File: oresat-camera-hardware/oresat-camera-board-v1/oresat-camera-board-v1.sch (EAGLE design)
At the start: 41 parts, among them J1 4-1734742-0, U1 AR0134CSSM00SPCA0, U2 TPS70618DRVR, U3 TPS71928-28DRVT, U4 TPS71928-28DRVT, X1 KC2520B27.0000C10E00

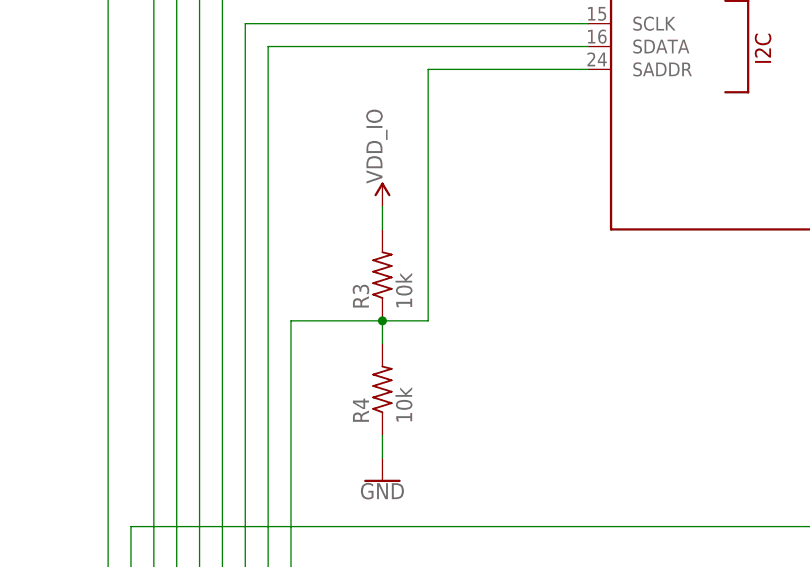
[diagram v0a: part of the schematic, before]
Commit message: small aesthetic changes
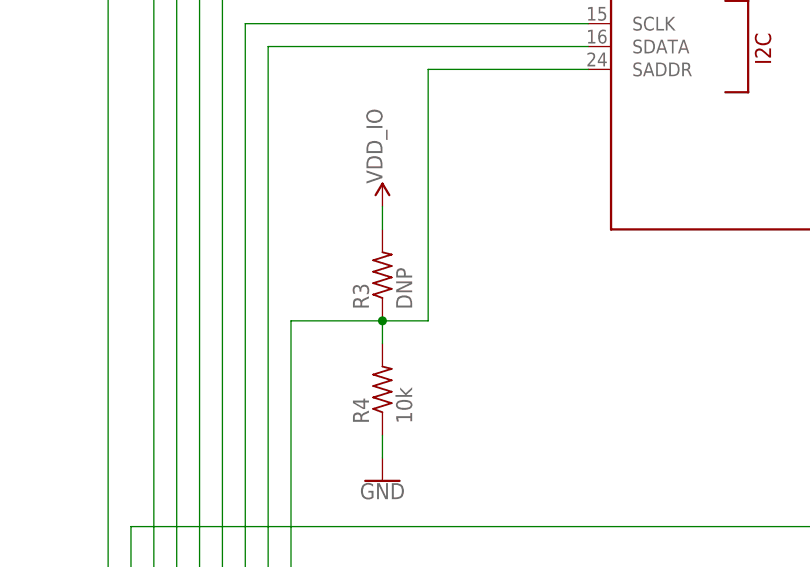
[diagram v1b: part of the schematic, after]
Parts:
- R3: value 10k -> DNP
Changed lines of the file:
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@@
 <part name="U1" library="U-ONSemi-AR0134" deviceset="AR0134CSSM00SPCA0" device=""/>
 <part name="GND6" library="SparkFun-PowerSymbols" deviceset="GND" device=""/>
-<part name="R3" library="oresat-rcl" deviceset="R-US_" device="0402-B" value="10k"/>
+<part name="R3" library="oresat-rcl" deviceset="R-US_" device="0402-B" value="DNP"/>
 <part name="SUPPLY3" library="SparkFun-PowerSymbols" deviceset="2.8V" device="" value="2.8V_1"/>
 <part name="R4" library="oresat-rcl" deviceset="R-US_" device="0402-B" value="10k"/>

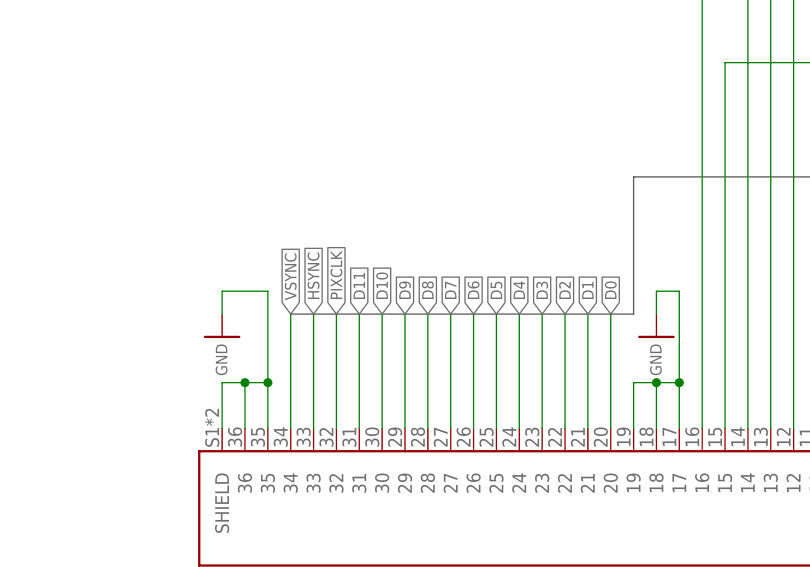
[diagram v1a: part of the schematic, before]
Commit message: rerouted camera bus
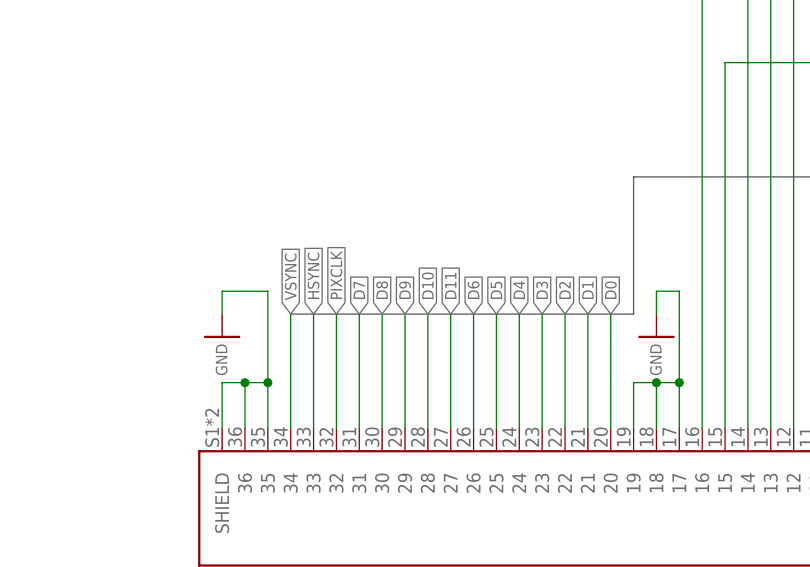
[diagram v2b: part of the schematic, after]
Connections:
- net D10: now also J1.28; no longer J1.30
- net D11: now also J1.27; no longer J1.31
- net D7: now also J1.31; no longer J1.27
- net D8: now also J1.30; no longer J1.28
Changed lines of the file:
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@@
 </segment>
 <segment>
-<pinref part="J1" gate="G$1" pin="27"/>
-<wire x1="109.22" y1="111.76" x2="109.22" y2="99.06" width="0.1524" layer="91"/>
-<label x="109.22" y="111.76" size="1.27" layer="95" rot="R90" xref="yes"/>
+<pinref part="J1" gate="G$1" pin="31"/>
+<wire x1="99.06" y1="111.76" x2="99.06" y2="99.06" width="0.1524" layer="91"/>
+<label x="99.06" y="111.76" size="1.27" layer="95" rot="R90" xref="yes"/>
 </segment>
 </net>
@@
 </segment>
 <segment>
-<pinref part="J1" gate="G$1" pin="28"/>
-<wire x1="106.68" y1="111.76" x2="106.68" y2="99.06" width="0.1524" layer="91"/>
-<label x="106.68" y="111.76" size="1.27" layer="95" rot="R90" xref="yes"/>
+<pinref part="J1" gate="G$1" pin="30"/>
+<wire x1="101.6" y1="111.76" x2="101.6" y2="99.06" width="0.1524" layer="91"/>
+<label x="101.6" y="111.76" size="1.27" layer="95" rot="R90" xref="yes"/>
 </segment>
 </net>
@@
 </segment>
 <segment>
-<pinref part="J1" gate="G$1" pin="30"/>
-<wire x1="101.6" y1="111.76" x2="101.6" y2="99.06" width="0.1524" layer="91"/>
-<label x="101.6" y="111.76" size="1.27" layer="95" rot="R90" xref="yes"/>
+<pinref part="J1" gate="G$1" pin="28"/>
+<wire x1="106.68" y1="111.76" x2="106.68" y2="99.06" width="0.1524" layer="91"/>
+<label x="106.68" y="111.76" size="1.27" layer="95" rot="R90" xref="yes"/>
 </segment>
 </net>
@@
 </segment>
 <segment>
-<pinref part="J1" gate="G$1" pin="31"/>
-<wire x1="99.06" y1="111.76" x2="99.06" y2="99.06" width="0.1524" layer="91"/>
-<label x="99.06" y="111.76" size="1.27" layer="95" rot="R90" xref="yes"/>
+<pinref part="J1" gate="G$1" pin="27"/>
+<wire x1="109.22" y1="111.76" x2="109.22" y2="99.06" width="0.1524" layer="91"/>
+<label x="109.22" y="111.76" size="1.27" layer="95" rot="R90" xref="yes"/>
 </segment>
 </net>

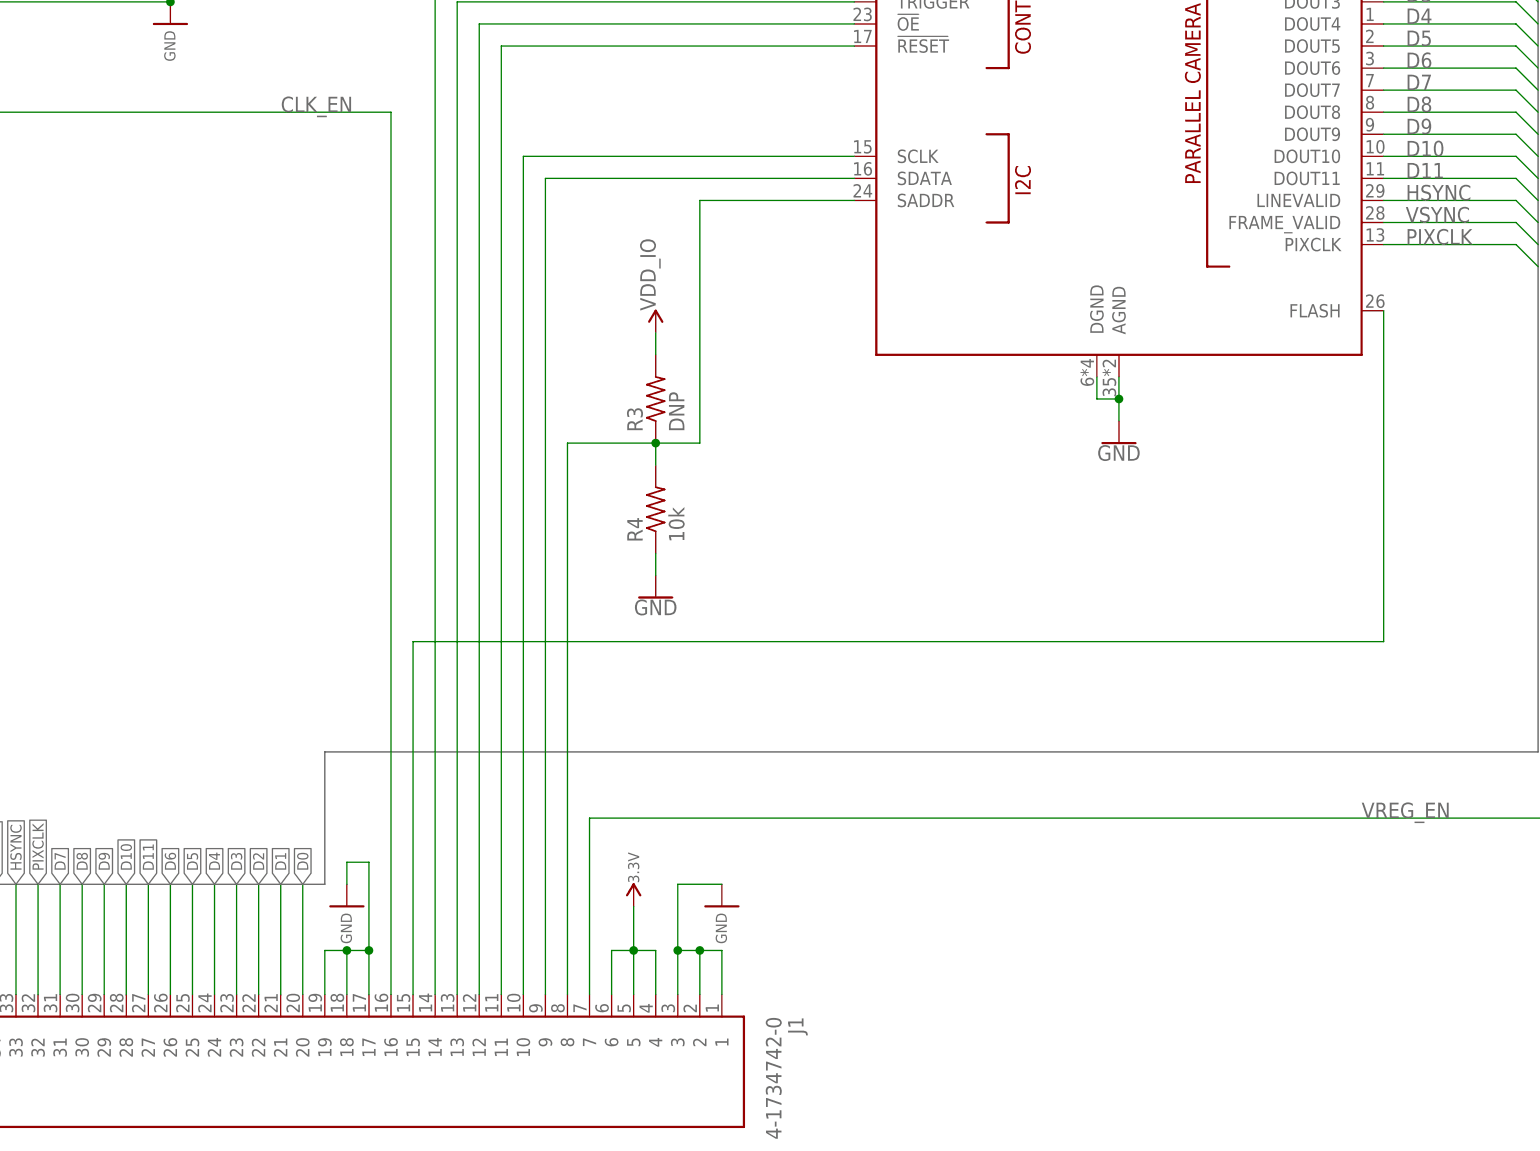
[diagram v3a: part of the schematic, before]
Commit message: added i2c pullups
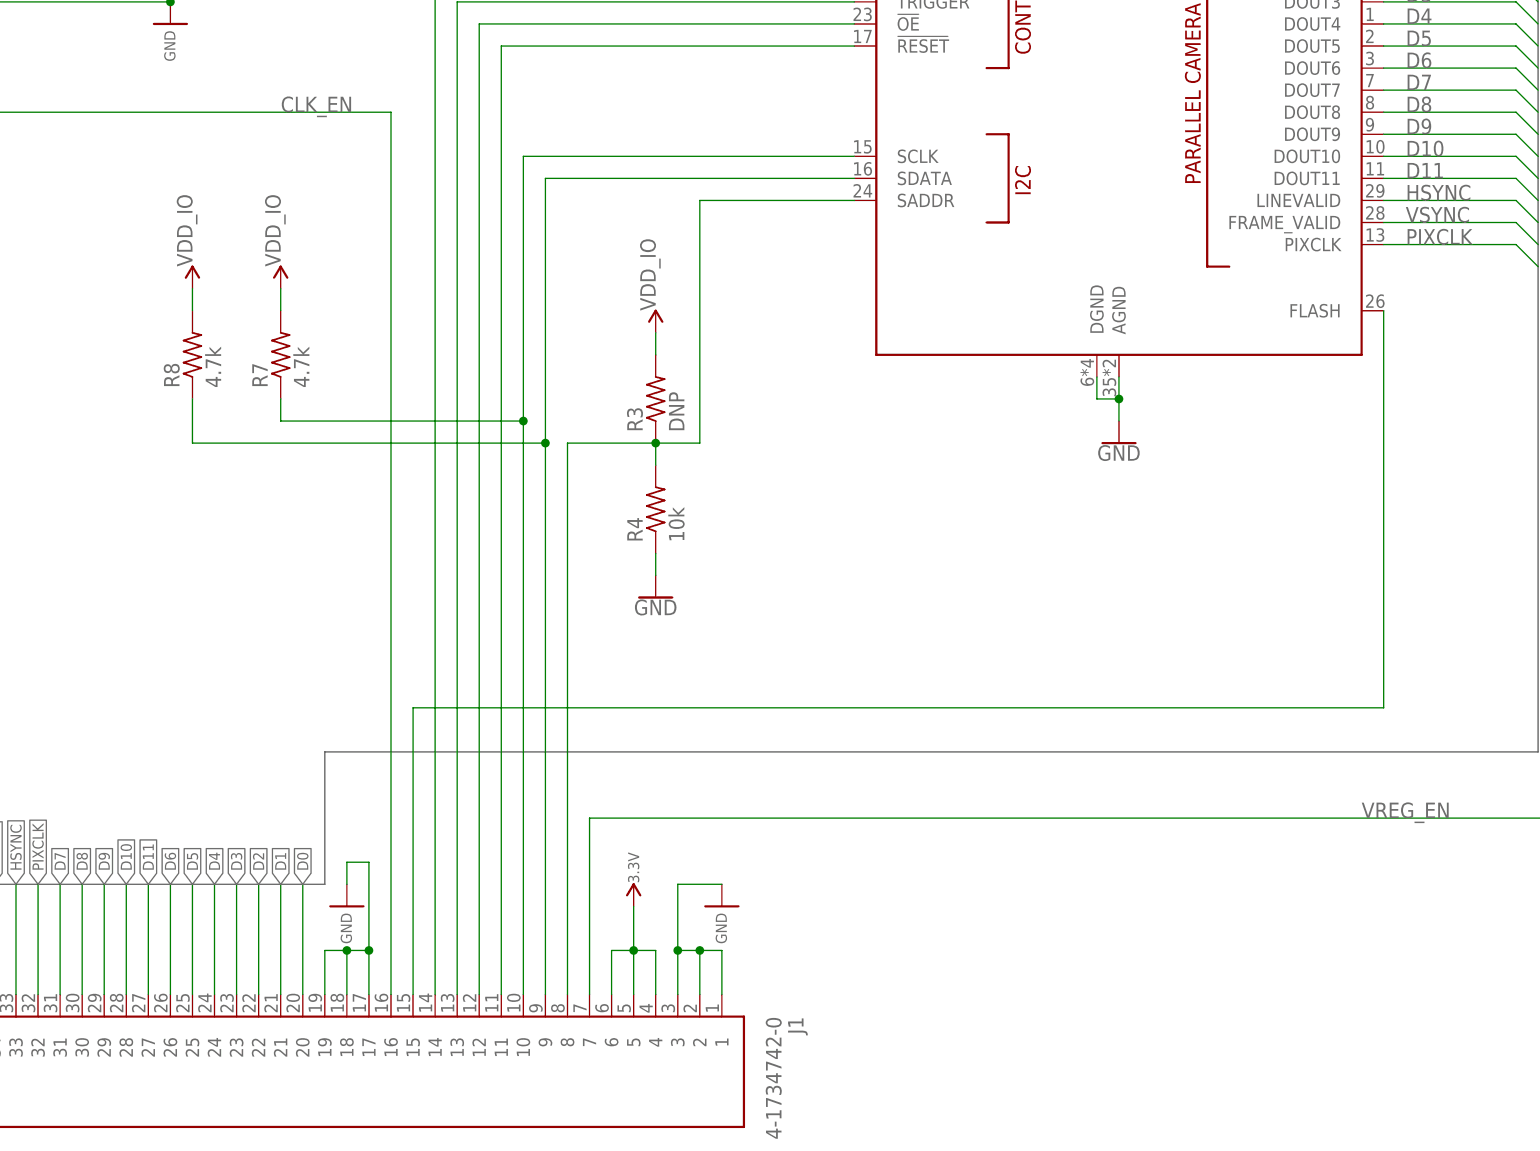
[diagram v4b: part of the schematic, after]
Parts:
- added R7, R8: 4.7k, oresat-rcl:R-US_0402-B
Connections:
- net N$3: now also R8.1
- net N$4: now also R7.1
- net VDD_IO: now also R7.2, R8.2
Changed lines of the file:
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@@
 <part name="SUPPLY27" library="SparkFun-PowerSymbols" deviceset="VCC_1" device="" value="2.8V_3"/>
 <part name="SUPPLY30" library="SparkFun-PowerSymbols" deviceset="VCC_2" device="" value="2.8V_4"/>
+<part name="R7" library="oresat-rcl" deviceset="R-US_" device="0402-B" value="4.7k"/>
+<part name="SUPPLY34" library="SparkFun-PowerSymbols" deviceset="2.8V" device="" value="2.8V_1"/>
+<part name="R8" library="oresat-rcl" deviceset="R-US_" device="0402-B" value="4.7k"/>
+<part name="SUPPLY35" library="SparkFun-PowerSymbols" deviceset="2.8V" device="" value="2.8V_1"/>
 </parts>
 <sheets>
@@
 <instance part="SUPPLY27" gate="G$2" x="327.66" y="248.92" smashed="yes"/>
 <instance part="SUPPLY30" gate="G$1" x="337.82" y="248.92" smashed="yes"/>
+<instance part="R7" gate="R" x="124.46" y="172.72" smashed="yes" rot="R90">
+<attribute name="NAME" x="122.9614" y="168.91" size="1.778" layer="95" rot="R90"/>
+<attribute name="VALUE" x="127.762" y="168.91" size="1.778" layer="96" rot="R90"/>
+</instance>
+<instance part="SUPPLY34" gate="G$1" x="124.46" y="180.34" smashed="yes"/>
+<instance part="R8" gate="R" x="114.3" y="172.72" smashed="yes" rot="R90">
+<attribute name="NAME" x="112.8014" y="168.91" size="1.778" layer="95" rot="R90"/>
+<attribute name="VALUE" x="117.602" y="168.91" size="1.778" layer="96" rot="R90"/>
+</instance>
+<instance part="SUPPLY35" gate="G$1" x="114.3" y="180.34" smashed="yes"/>
 </instances>
 <busses>
@@
 <label x="112.268" y="247.142" size="1.27" layer="95" rot="R90"/>
 </segment>
+<segment>
+<pinref part="SUPPLY34" gate="G$1" pin="2.8V"/>
+<pinref part="R7" gate="R" pin="2"/>
+<wire x1="124.46" y1="180.34" x2="124.46" y2="177.8" width="0.1524" layer="91"/>
+<label x="124.46" y="182.88" size="1.778" layer="95" rot="R90"/>
+</segment>
+<segment>
+<pinref part="SUPPLY35" gate="G$1" pin="2.8V"/>
+<pinref part="R8" gate="R" pin="2"/>
+<wire x1="114.3" y1="180.34" x2="114.3" y2="177.8" width="0.1524" layer="91"/>
+<label x="114.3" y="182.88" size="1.778" layer="95" rot="R90"/>
+</segment>
 </net>
 <net name="VAA" class="0">
@@
 <pinref part="J1" gate="G$1" pin="9"/>
 <wire x1="190.5" y1="193.04" x2="154.94" y2="193.04" width="0.1524" layer="91"/>
-<wire x1="154.94" y1="193.04" x2="154.94" y2="99.06" width="0.1524" layer="91"/>
+<wire x1="154.94" y1="193.04" x2="154.94" y2="162.56" width="0.1524" layer="91"/>
+<pinref part="R8" gate="R" pin="1"/>
+<wire x1="154.94" y1="162.56" x2="154.94" y2="99.06" width="0.1524" layer="91"/>
+<wire x1="154.94" y1="162.56" x2="114.3" y2="162.56" width="0.1524" layer="91"/>
+<wire x1="114.3" y1="162.56" x2="114.3" y2="167.64" width="0.1524" layer="91"/>
+<junction x="154.94" y="162.56"/>
 </segment>
 </net>
@@
 <pinref part="J1" gate="G$1" pin="10"/>
 <wire x1="190.5" y1="195.58" x2="152.4" y2="195.58" width="0.1524" layer="91"/>
-<wire x1="152.4" y1="195.58" x2="152.4" y2="99.06" width="0.1524" layer="91"/>
+<wire x1="152.4" y1="195.58" x2="152.4" y2="165.1" width="0.1524" layer="91"/>
+<pinref part="R7" gate="R" pin="1"/>
+<wire x1="152.4" y1="165.1" x2="152.4" y2="99.06" width="0.1524" layer="91"/>
+<wire x1="124.46" y1="167.64" x2="124.46" y2="165.1" width="0.1524" layer="91"/>
+<wire x1="124.46" y1="165.1" x2="152.4" y2="165.1" width="0.1524" layer="91"/>
+<junction x="152.4" y="165.1"/>
 </segment>
 </net>
@@
 <segment>
 <pinref part="U1" gate="G$1" pin="FLASH"/>
-<wire x1="251.46" y1="177.8" x2="251.46" y2="139.7" width="0.1524" layer="91"/>
-<wire x1="251.46" y1="139.7" x2="139.7" y2="139.7" width="0.1524" layer="91"/>
+<wire x1="251.46" y1="177.8" x2="251.46" y2="132.08" width="0.1524" layer="91"/>
+<wire x1="251.46" y1="132.08" x2="139.7" y2="132.08" width="0.1524" layer="91"/>
 <pinref part="J1" gate="G$1" pin="15"/>
-<wire x1="139.7" y1="139.7" x2="139.7" y2="99.06" width="0.1524" layer="91"/>
+<wire x1="139.7" y1="132.08" x2="139.7" y2="99.06" width="0.1524" layer="91"/>
 </segment>
 </net>
@@
 </sheet>
 </sheets>
+<errors>
+</errors>
 </schematic>
 </drawing>
